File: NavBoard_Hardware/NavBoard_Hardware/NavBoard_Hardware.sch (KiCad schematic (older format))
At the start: 48 parts

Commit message: Finished wiring BNO080 circuit
Also changed values of indicator resistors
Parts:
- added C? (x3): 100nF, symbol Device:C
- added D? (x2): BLUE, symbol Device:LED
- added R? (x2): 100, symbol Device:R
- added R? (x3): 10k, symbol Device:R
- AC?: symbol BNO080:BNO080 -> NavBoard_Hardware-rescue:BNO080-BNO080
- Conn? (x2): symbol MRDT_Connectors:AndersonPP -> NavBoard_Hardware-rescue:AndersonPP-MRDT_Connectors
- Conn?: symbol MRDT_Connectors:RP-SMA -> NavBoard_Hardware-rescue:RP-SMA-MRDT_Connectors
- R? (x9): value 520 -> 100
- R?: value 330 -> 43
- U?: symbol MRDT_Shields:Raspberry_Pi -> NavBoard_Hardware-rescue:Raspberry_Pi-MRDT_Shields
- U?: symbol MRDT_ICs:NEO-M8P-2 -> NavBoard_Hardware-rescue:NEO-M8P-2-MRDT_ICs
- U?: symbol MRDT_ICs:ICM-20948 -> NavBoard_Hardware-rescue:ICM-20948-MRDT_ICs
- U?: symbol MRDT_ICs:BNO055 -> NavBoard_Hardware-rescue:BNO055-MRDT_ICs
- U? (x2): symbol MRDT_Devices:OKI -> NavBoard_Hardware-rescue:OKI-MRDT_Devices
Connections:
- net labels added: BNO080_RX, BNO080_TX
- wire segments 192 -> 248
- no-connect marks 39 -> 51
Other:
- moved on the sheet: C?

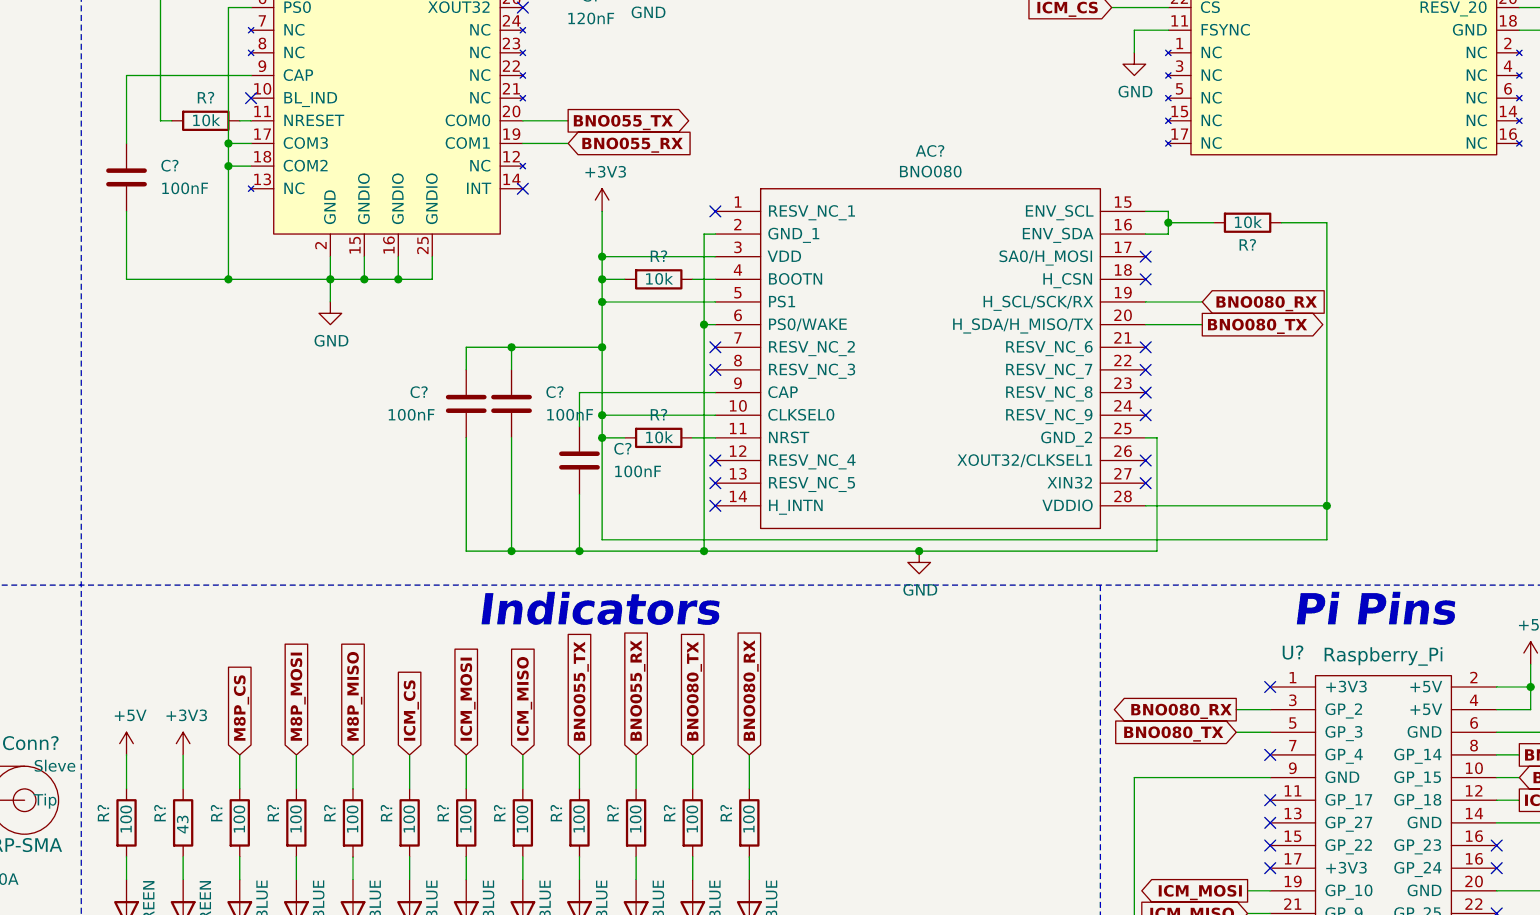
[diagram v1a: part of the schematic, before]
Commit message: Changed BNO080 to I2C communication
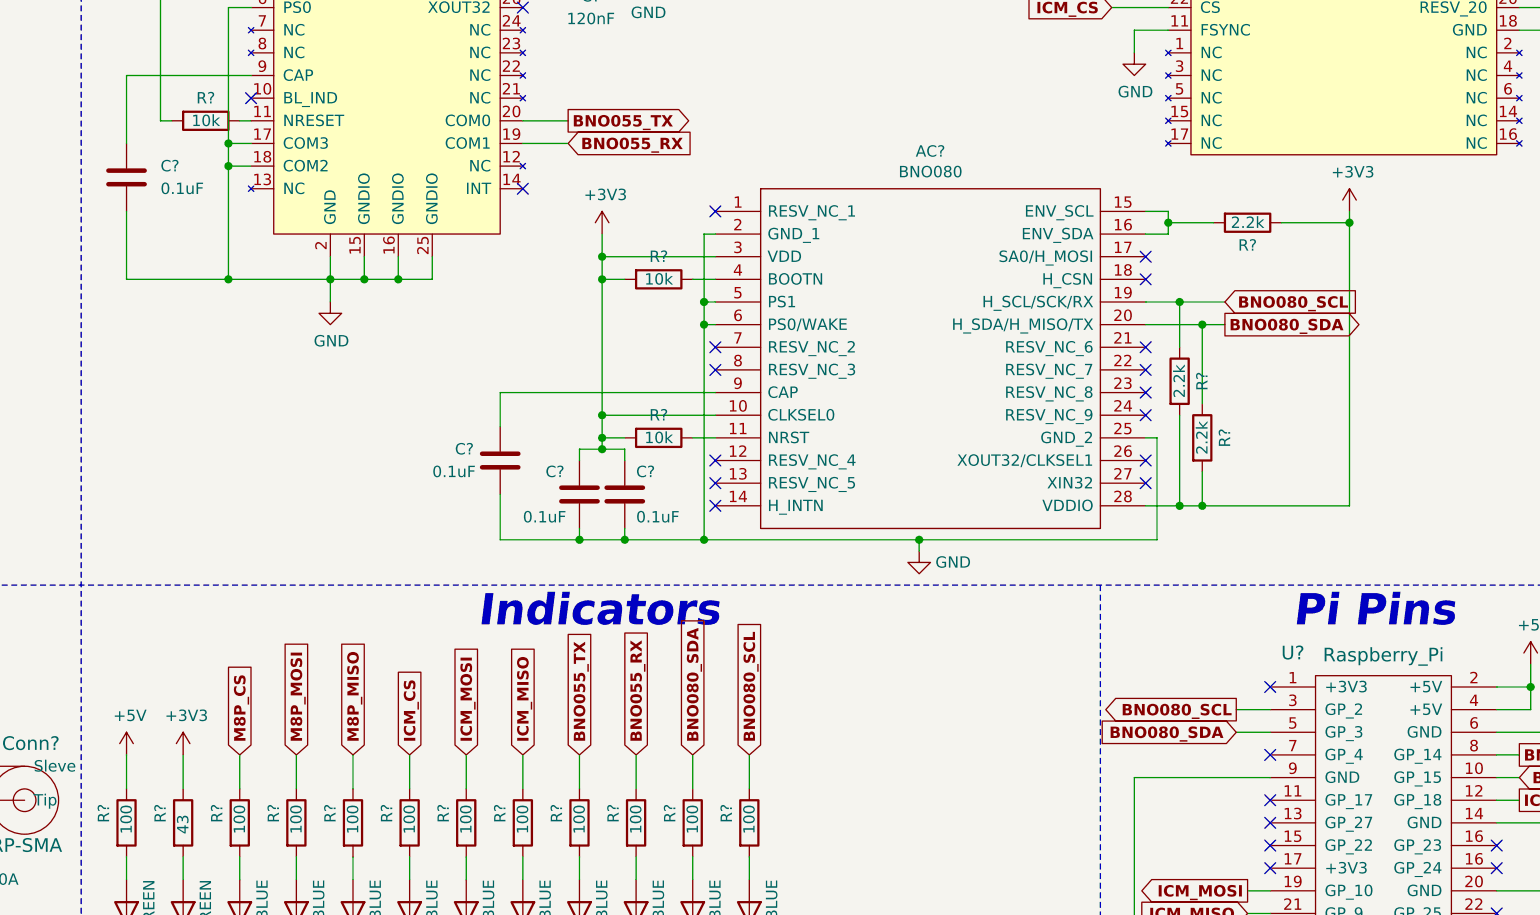
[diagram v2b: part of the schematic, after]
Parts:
- added R? (x2): 2.2k, symbol Device:R
- C? (x4): value 100nF -> 0.1uF
- R?: value 10k -> 2.2k
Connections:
- net +3V3: now also R?.2, R?.2; no longer AC?.5 (PS1)
- net GND: now also AC?.5 (PS1)
- net BNO080_RX renamed BNO080_SCL
- net BNO080_SCL: now also R?.1
- net BNO080_TX renamed BNO080_SDA
- net BNO080_SDA: now also R?.1
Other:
- moved on the sheet: C?
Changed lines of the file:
@@
 P 4350 2100
 F 0 "C?" H 4500 2150 50  0000 L CNN
-F 1 "100nF" H 4500 2050 50  0000 L CNN
+F 1 "0.1uF" H 4500 2050 50  0000 L CNN
 F 2 "" H 4388 1950 50  0001 C CNN
 F 3 "~" H 4350 2100 50  0001 C CNN
@@
 P 7850 3750
 F 0 "#PWR?" H 7850 3500 50  0001 C CNN
-F 1 "GND" H 7855 3577 50  0000 C CNN
+F 1 "GND" H 8000 3700 50  0000 C CNN
 F 2 "" H 7850 3750 50  0001 C CNN
 F 3 "" H 7850 3750 50  0001 C CNN
@@
 Wire Wire Line
 	8850 3250 8900 3250
-Wire Wire Line
-	8900 3250 8900 3750
-Connection ~ 7850 3750
-Wire Wire Line
-	8900 3750 7850 3750
 $Comp
 L power:+3V3 #PWR?
 U 1 1 616AB537
-P 6450 2250
-F 0 "#PWR?" H 6450 2100 50  0001 C CNN
-F 1 "+3V3" H 6465 2423 50  0000 C CNN
-F 2 "" H 6450 2250 50  0001 C CNN
-F 3 "" H 6450 2250 50  0001 C CNN
-	1    6450 2250
+P 6450 2350
+F 0 "#PWR?" H 6450 2200 50  0001 C CNN
+F 1 "+3V3" H 6465 2523 50  0000 C CNN
+F 2 "" H 6450 2350 50  0001 C CNN
+F 3 "" H 6450 2350 50  0001 C CNN
+	1    6450 2350
 	1    0    0    -1
 $EndComp
@@
 Text GLabel 6300 1950 2    50   Input ~ 10
 BNO055_RX
-Text GLabel 9100 2750 2    50   Output ~ 10
-BNO080_TX
-Text GLabel 9100 2650 2    50   Input ~ 10
-BNO080_RX
-Wire Wire Line
-	9100 2650 8850 2650
-Wire Wire Line
-	9100 2750 8850 2750
+Text GLabel 9200 2750 2    50   Output ~ 10
+BNO080_SDA
+Text GLabel 9200 2650 2    50   Input ~ 10
+BNO080_SCL
 Wire Wire Line
 	9400 4450 9250 4450
 Text GLabel 9250 4450 0    50   Output ~ 10
-BNO080_RX
+BNO080_SCL
 Wire Wire Line
 	9250 4550 9400 4550
 Text GLabel 9250 4550 0    50   Input ~ 10
-BNO080_TX
+BNO080_SDA
 Text GLabel 6850 4650 1    50   Input ~ 10
-BNO080_TX
+BNO080_SDA
 Text GLabel 7100 4650 1    50   Input ~ 10
-BNO080_RX
+BNO080_SCL
 $Comp
 L power:GND #PWR?
@@
 L Device:C C?
 U 1 1 618FFFD8
-P 6350 3350
-F 0 "C?" H 6500 3400 50  0000 L CNN
-F 1 "100nF" H 6500 3300 50  0000 L CNN
-F 2 "" H 6388 3200 50  0001 C CNN
-F 3 "~" H 6350 3350 50  0001 C CNN
-	1    6350 3350
-	1    0    0    -1
-$EndComp
-Wire Wire Line
-	6350 3200 6350 3050
-Wire Wire Line
-	6350 3050 6950 3050
-Wire Wire Line
-	6350 3500 6350 3750
+P 6000 3350
+F 0 "C?" H 5800 3400 50  0000 L CNN
+F 1 "0.1uF" H 5700 3300 50  0000 L CNN
+F 2 "" H 6038 3200 50  0001 C CNN
+F 3 "~" H 6000 3350 50  0001 C CNN
+	1    6000 3350
+	1    0    0    -1
+$EndComp
 $Comp
 L Device:R R?
@@
 	6450 3150 6950 3150
 Wire Wire Line
-	6450 2250 6450 2450
-Wire Wire Line
-	6900 2350 6900 2750
+	6450 2350 6450 2450
+Wire Wire Line
+	6900 2350 6900 2650
 Wire Wire Line
 	6950 2450 6450 2450
@@
 Wire Wire Line
 	6850 3250 6950 3250
-Connection ~ 6900 3750
-Wire Wire Line
-	6900 3750 7850 3750
-Wire Wire Line
-	6350 3750 6900 3750
 $Comp
 L Device:R R?
@@
 Connection ~ 6450 2550
 Wire Wire Line
-	6450 2550 6450 2650
-Wire Wire Line
-	6950 2650 6450 2650
-Connection ~ 6450 2650
-Wire Wire Line
-	6450 2650 6450 2850
-Wire Wire Line
 	6950 2750 6900 2750
 Connection ~ 6900 2750
 Wire Wire Line
-	6900 2750 6900 3750
+	6900 2750 6900 3700
 NoConn ~ 6950 2250
 NoConn ~ 6950 2850
@@
 NoConn ~ 8850 2550
 NoConn ~ 8850 2450
-Wire Wire Line
-	6450 3700 6450 3250
-Connection ~ 6450 3250
 $Comp
 L Device:R R?
@@
 P 9300 2300
 F 0 "R?" V 9400 2300 50  0000 C CNN
-F 1 "10k" V 9300 2300 50  0000 C CNN
+F 1 "2.2k" V 9300 2300 50  0000 C CNN
 F 2 "" V 9230 2300 50  0001 C CNN
 F 3 "~" H 9300 2300 50  0001 C CNN
@@
 	8850 2350 8950 2350
 Wire Wire Line
-	6450 3700 9650 3700
-Wire Wire Line
-	8850 3550 9650 3550
-Wire Wire Line
-	9650 3550 9650 3700
-Wire Wire Line
-	9650 3550 9650 2300
-Connection ~ 9650 3550
-Wire Wire Line
 	8950 2250 8950 2300
 Wire Wire Line
@@
 	8950 2350 8950 2300
 Connection ~ 8950 2300
-Wire Wire Line
-	9450 2300 9650 2300
 NoConn ~ 6950 3550
 NoConn ~ 8850 3350
 NoConn ~ 8850 3450
+Wire Wire Line
+	10400 5750 11050 5750
+Connection ~ 11050 5750
+Wire Wire Line
+	11050 5750 11050 5950
+Wire Wire Line
+	6950 2650 6900 2650
+Connection ~ 6900 2650
+Wire Wire Line
+	6900 2650 6900 2750
+Wire Wire Line
+	9450 2300 9750 2300
+Wire Wire Line
+	8850 3550 9000 3550
+Wire Wire Line
+	8850 2650 9000 2650
+Wire Wire Line
+	8850 2750 9100 2750
+$Comp
+L Device:R R?
+U 1 1 61788B9D
+P 9000 3000
+F 0 "R?" V 9100 3000 50  0000 C CNN
+F 1 "2.2k" V 9000 3000 50  0000 C CNN
+F 2 "" V 8930 3000 50  0001 C CNN
+F 3 "~" H 9000 3000 50  0001 C CNN
+	1    9000 3000
+	1    0    0    -1
+$EndComp
+$Comp
+L Device:R R?
+U 1 1 6179688A
+P 9100 3250
+F 0 "R?" V 9200 3250 50  0000 C CNN
+F 1 "2.2k" V 9100 3250 50  0000 C CNN
+F 2 "" V 9030 3250 50  0001 C CNN
+F 3 "~" H 9100 3250 50  0001 C CNN
+	1    9100 3250
+	1    0    0    -1
+$EndComp
+Wire Wire Line
+	9000 2850 9000 2650
+Connection ~ 9000 2650
+Wire Wire Line
+	9000 2650 9200 2650
+Wire Wire Line
+	9100 3100 9100 2750
+Connection ~ 9100 2750
+Wire Wire Line
+	9100 2750 9200 2750
+Wire Wire Line
+	9000 3150 9000 3550
+Connection ~ 9000 3550
+Wire Wire Line
+	9100 3400 9100 3550
+Wire Wire Line
+	9000 3550 9100 3550
+Connection ~ 9100 3550
+Wire Wire Line
+	9100 3550 9750 3550
+$Comp
+L power:+3V3 #PWR?
+U 1 1 617DDE06
+P 9750 2250
+F 0 "#PWR?" H 9750 2100 50  0001 C CNN
+F 1 "+3V3" H 9765 2423 50  0000 C CNN
+F 2 "" H 9750 2250 50  0001 C CNN
+F 3 "" H 9750 2250 50  0001 C CNN
+	1    9750 2250
+	1    0    0    -1
+$EndComp
+Wire Wire Line
+	9750 2250 9750 2300
+Connection ~ 9750 2300
+Wire Wire Line
+	9750 2300 9750 3550
+Wire Wire Line
+	8900 3250 8900 3700
+Wire Wire Line
+	8900 3700 7850 3700
+Wire Wire Line
+	7850 3750 7850 3700
+Connection ~ 7850 3700
+Wire Wire Line
+	7850 3700 6900 3700
+Wire Wire Line
+	6000 3500 6000 3700
+Connection ~ 6900 3700
+$Comp
+L Device:C C?
+U 1 1 61C227E5
+P 6550 3500
+F 0 "C?" H 6600 3600 50  0000 L CNN
+F 1 "0.1uF" H 6600 3400 50  0000 L CNN
+F 2 "" H 6588 3350 50  0001 C CNN
+F 3 "~" H 6550 3500 50  0001 C CNN
+	1    6550 3500
+	1    0    0    -1
+$EndComp
 $Comp
 L Device:C C?
 U 1 1 61C14F96
-P 5850 3100
-F 0 "C?" H 5600 3150 50  0000 L CNN
-F 1 "100nF" H 5500 3050 50  0000 L CNN
-F 2 "" H 5888 2950 50  0001 C CNN
-F 3 "~" H 5850 3100 50  0001 C CNN
-	1    5850 3100
-	1    0    0    -1
-$EndComp
-$Comp
-L Device:C C?
-U 1 1 61C227E5
-P 6050 3100
-F 0 "C?" H 6200 3150 50  0000 L CNN
-F 1 "100nF" H 6200 3050 50  0000 L CNN
-F 2 "" H 6088 2950 50  0001 C CNN
-F 3 "~" H 6050 3100 50  0001 C CNN
-	1    6050 3100
-	1    0    0    -1
-$EndComp
-Wire Wire Line
-	5850 2950 5850 2850
-Wire Wire Line
-	5850 2850 6050 2850
-Connection ~ 6450 2850
-Wire Wire Line
-	6450 2850 6450 3150
-Wire Wire Line
-	6050 2950 6050 2850
-Connection ~ 6050 2850
-Wire Wire Line
-	6050 2850 6450 2850
-Wire Wire Line
-	5850 3250 5850 3750
-Connection ~ 6350 3750
-Wire Wire Line
-	6050 3250 6050 3750
-Wire Wire Line
-	5850 3750 6050 3750
-Connection ~ 6050 3750
-Wire Wire Line
-	6050 3750 6350 3750
-Wire Wire Line
-	10400 5750 11050 5750
-Connection ~ 11050 5750
-Wire Wire Line
-	11050 5750 11050 5950
+P 6350 3500
+F 0 "C?" H 6200 3600 50  0000 L CNN
+F 1 "0.1uF" H 6100 3400 50  0000 L CNN
+F 2 "" H 6388 3350 50  0001 C CNN
+F 3 "~" H 6350 3500 50  0001 C CNN
+	1    6350 3500
+	1    0    0    -1
+$EndComp
+Wire Wire Line
+	6450 3250 6450 3300
+Wire Wire Line
+	6450 3300 6550 3300
+Wire Wire Line
+	6550 3300 6550 3350
+Connection ~ 6450 3250
+Wire Wire Line
+	6450 3300 6350 3300
+Wire Wire Line
+	6350 3300 6350 3350
+Connection ~ 6450 3300
+Wire Wire Line
+	6350 3650 6350 3700
+Wire Wire Line
+	6350 3700 6550 3700
+Wire Wire Line
+	6550 3650 6550 3700
+Connection ~ 6550 3700
+Wire Wire Line
+	6550 3700 6900 3700
+Wire Wire Line
+	6450 2550 6450 3150
+Wire Wire Line
+	6950 3050 6000 3050
+Wire Wire Line
+	6000 3050 6000 3200
+Wire Wire Line
+	6000 3700 6350 3700
+Connection ~ 6350 3700
 $EndSCHEMATC

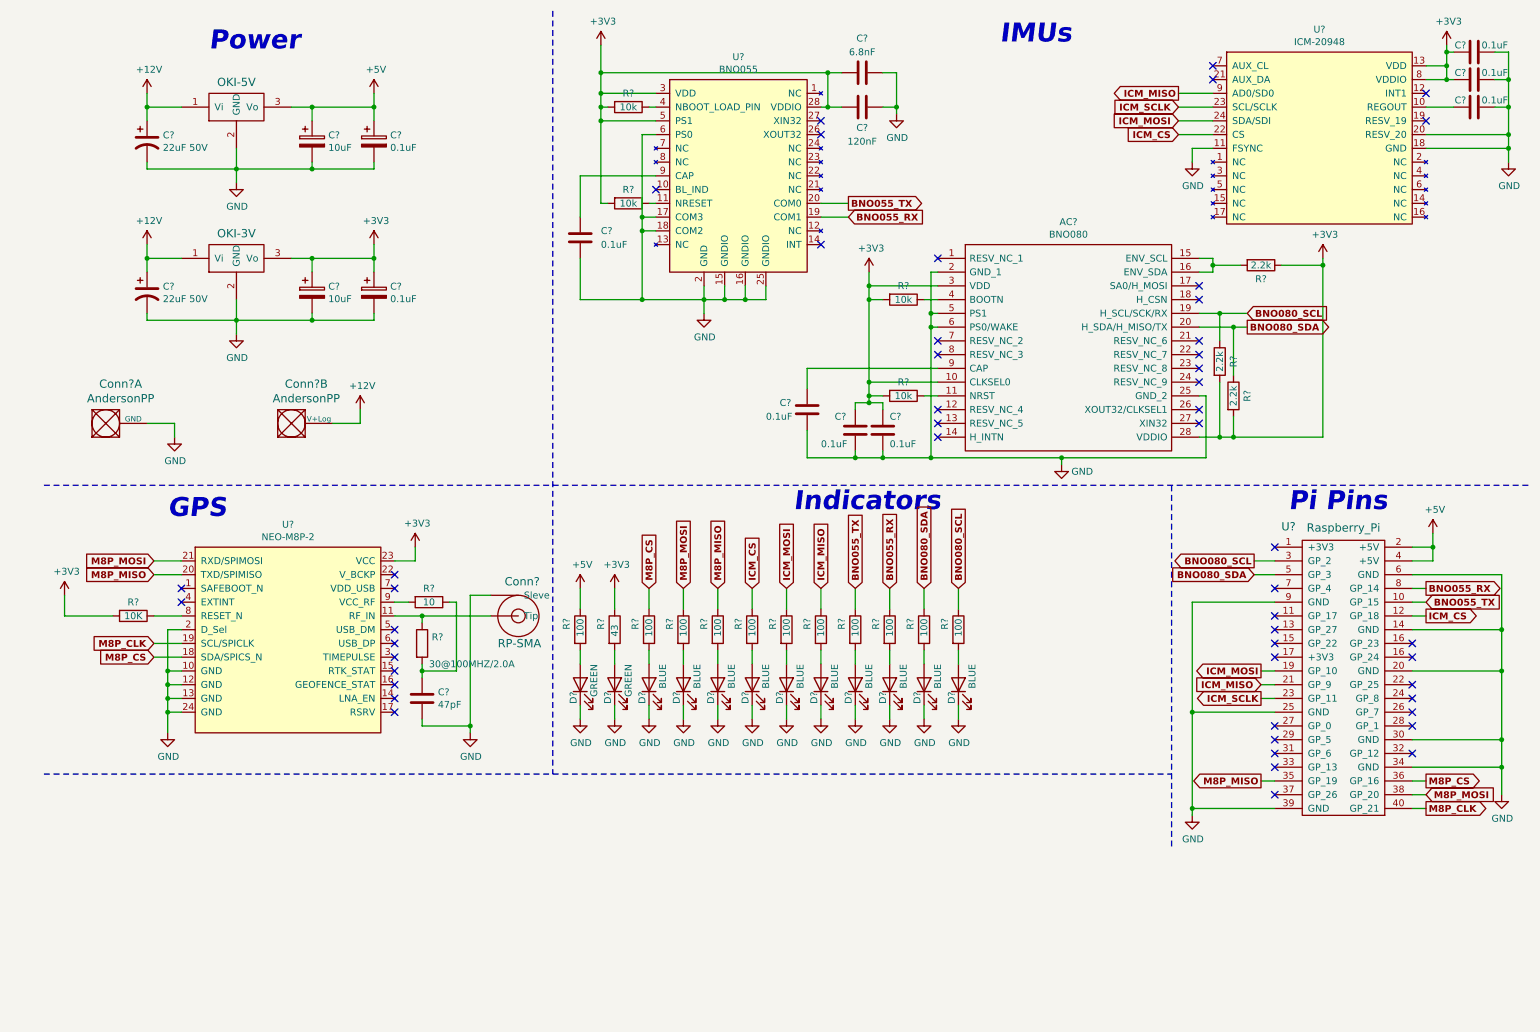
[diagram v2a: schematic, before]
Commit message: Added backup battery for GPS
Change was discussed in PDR. Also fixed input to BNO080.
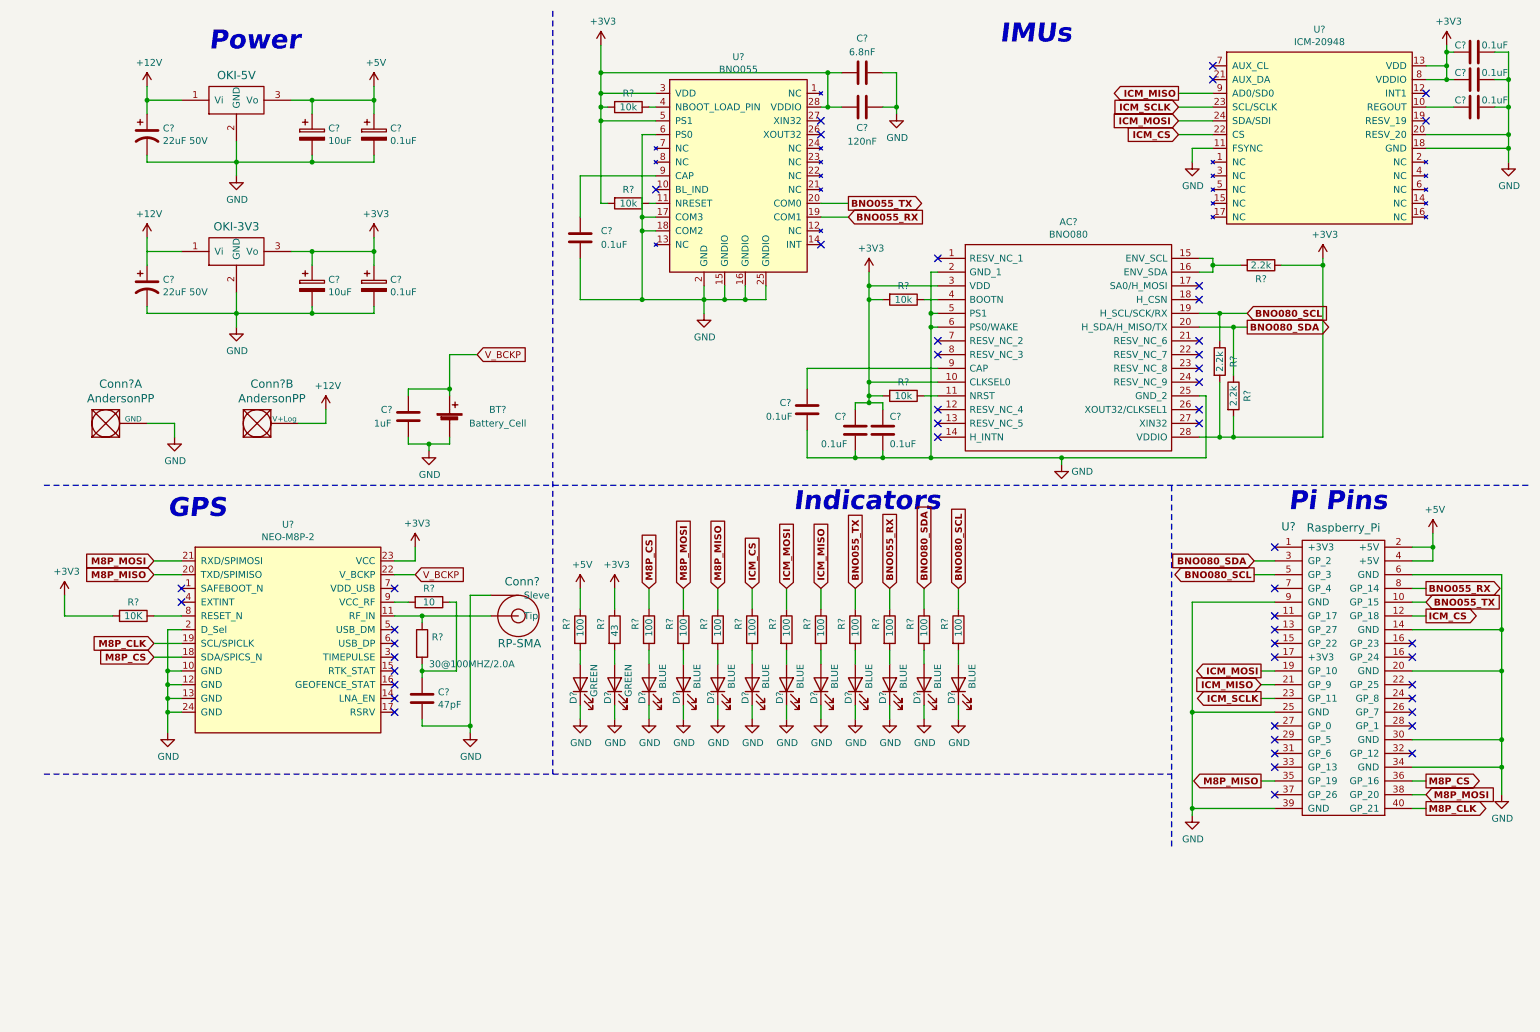
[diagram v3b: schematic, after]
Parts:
- added BT?: Battery_Cell, symbol Device:Battery_Cell
- added C?: 1uF, symbol Device:C
- U?: value OKI-3V -> OKI-3V3
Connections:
- net BNO080_SCL: now also U?.5 (GP_3); no longer U?.3 (GP_2)
- net BNO080_SDA: now also U?.3 (GP_2); no longer U?.5 (GP_3)
- net GND: now also BT?.2 (-), C?.2
- net V_BCKP: now reaches U?.22 (V_BCKP)
- net V_BCKP: now also BT?.1 (+), C?.1
- no-connect marks 51 -> 50
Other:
- moved on the sheet: C?, Conn?B
